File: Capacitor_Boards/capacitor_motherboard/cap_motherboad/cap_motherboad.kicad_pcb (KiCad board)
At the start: 2 copper layers, 180.5 x 92 mm, 14 parts, among them J1 Conn_01x02_Female, J10 Conn_01x02_Female, J11 Conn_01x02_Female, J12 Conn_01x02_Female, J2 Conn_01x02_Female, J3 Conn_01x02_Female, J4 Conn_01x02_Female, J5 Conn_01x02_Female, J6 Conn_01x02_Female, J7 Conn_01x02_Female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

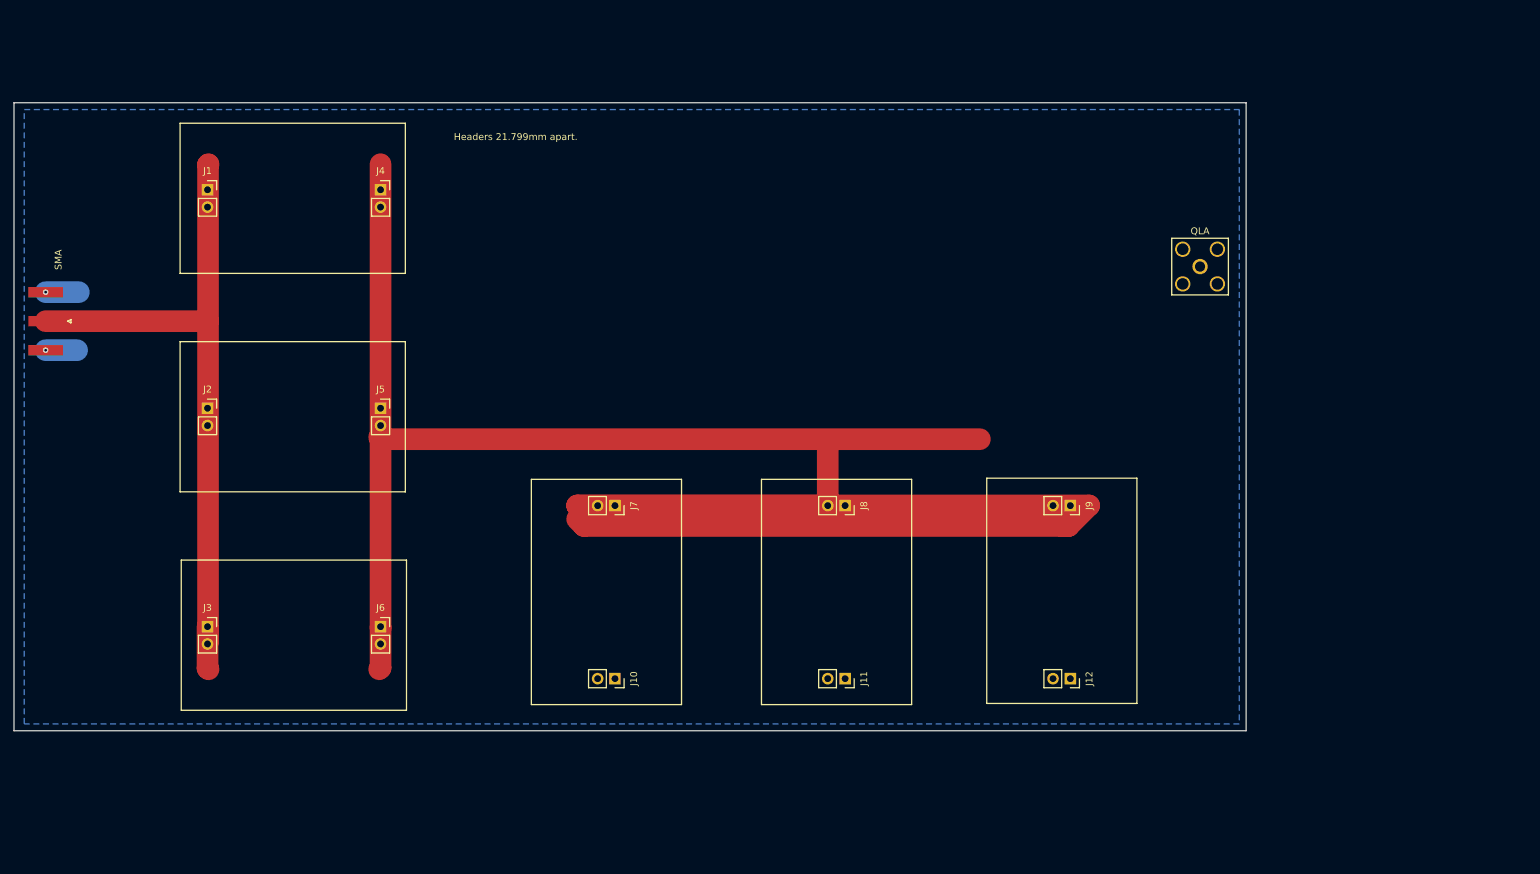
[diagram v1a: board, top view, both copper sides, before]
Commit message: Connected the QLA  connector
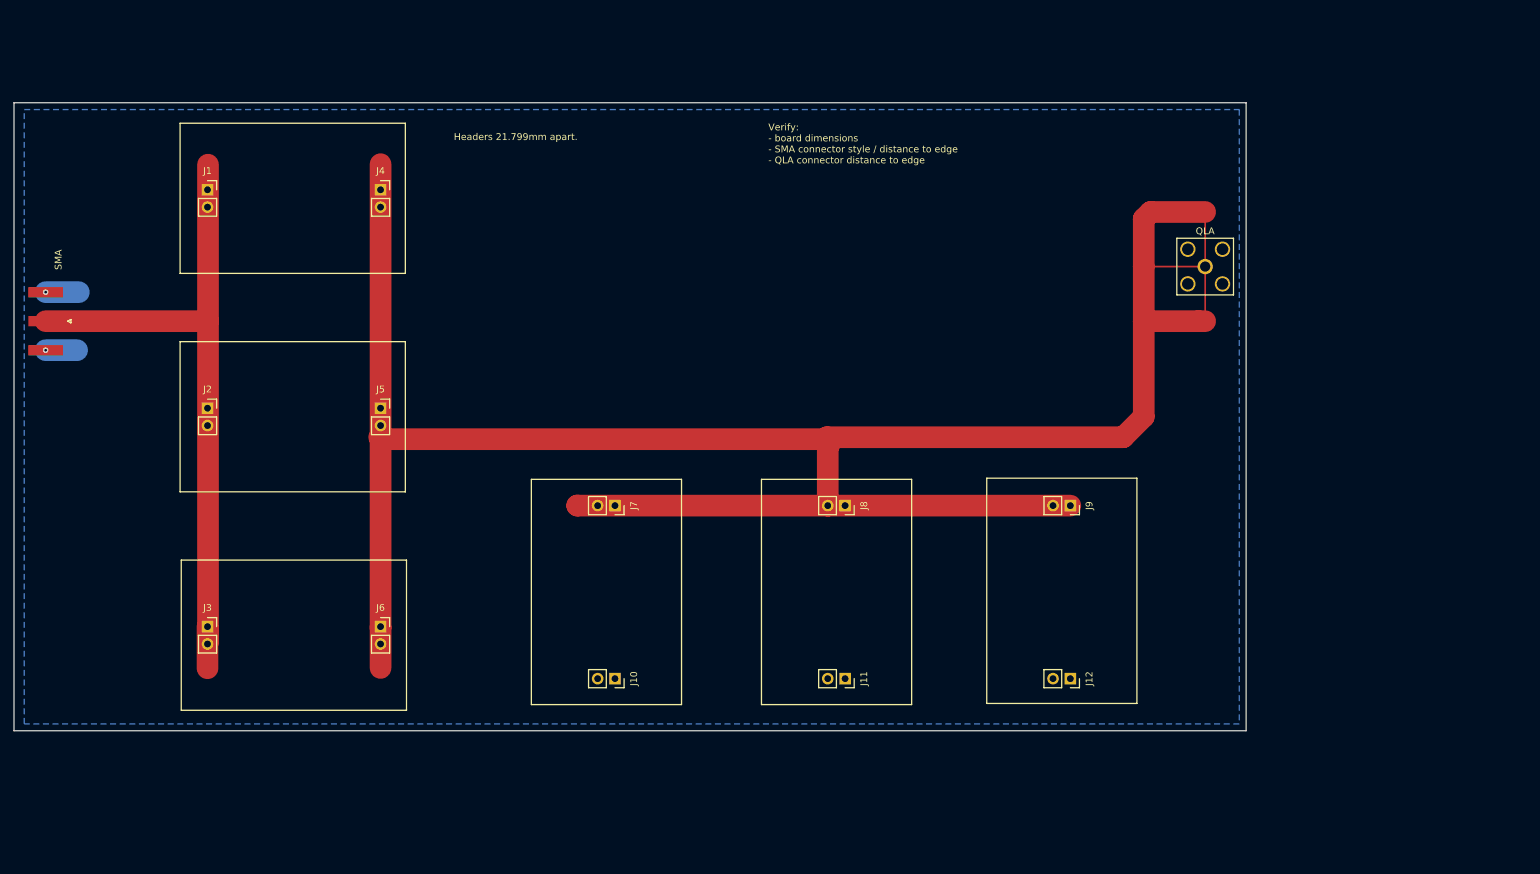
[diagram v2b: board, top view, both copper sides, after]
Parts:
- moved QLA 0.75 mm to (204.0, 62.0)
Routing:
- net Net-(J4-Pad1): track 359.6 -> 340.9 mm
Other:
- board text added: "Verify: - board dimensions - SMA connector style / distance to edge - QLA connector distance to edge"
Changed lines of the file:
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@@
   )
   (footprint "Connector_Coaxial:SMA_Amphenol_132203-12_Horizontal" (layer "F.Cu")
-    (at 203.25 62 -90)
+    (at 204 62 -90)
     (descr "https://www.amphenolrf.com/media/downloads/1769/132203-12.pdf")
     (tags "SMA THT Female Jack Horizontal")
@@
     (fp_line (start -3.175 -19.5) (end 3.175 -19.5) (layer "F.Fab") (width 0.1))
     (fp_line (start -3.175 -18) (end 3.175 -18.706) (layer "F.Fab") (width 0.1))
-    (pad "1" thru_hole circle (at 0 0 270) (size 2.25 2.25) (drill 1.5) (layers *.Cu *.Mask)
+    (pad "1" thru_hole circle (at 0 0 270) (size 2.25 2.25) (drill 1.5) (layers *.Cu *.Mask) (remove_unused_layers)
       (net 1 "Net-(J4-Pad1)") (pinfunction "In") (pintype "passive"))
-    (pad "2" thru_hole circle (at -2.54 -2.54 270) (size 2.25 2.25) (drill 1.7) (layers *.Cu *.Mask)
+    (pad "2" thru_hole circle (at -2.54 -2.54 270) (size 2.25 2.25) (drill 1.7) (layers *.Cu *.Mask) (remove_unused_layers)
       (net 2 "GND") (pinfunction "Ext") (pintype "passive"))
-    (pad "2" thru_hole circle (at 2.54 2.54) (size 2.25 2.25) (drill 1.7) (layers *.Cu *.Mask)
+    (pad "2" thru_hole circle (at 2.54 2.54) (size 2.25 2.25) (drill 1.7) (layers *.Cu *.Mask) (remove_unused_layers)
       (net 2 "GND") (pinfunction "Ext") (pintype "passive"))
-    (pad "2" thru_hole circle (at 2.54 -2.54 270) (size 2.25 2.25) (drill 1.7) (layers *.Cu *.Mask)
+    (pad "2" thru_hole circle (at 2.54 -2.54 270) (size 2.25 2.25) (drill 1.7) (layers *.Cu *.Mask) (remove_unused_layers)
       (net 2 "GND") (pinfunction "Ext") (pintype "passive"))
-    (pad "2" thru_hole circle (at -2.54 2.54 270) (size 2.25 2.25) (drill 1.7) (layers *.Cu *.Mask)
+    (pad "2" thru_hole circle (at -2.54 2.54 270) (size 2.25 2.25) (drill 1.7) (layers *.Cu *.Mask) (remove_unused_layers)
       (net 2 "GND") (pinfunction "Ext") (pintype "passive"))
     (model "${KICAD6_3DMODEL_DIR}/Connector_Coaxial.3dshapes/SMA_Amphenol_132203-12_Horizontal.wrl"
@@
   (gr_rect (start 53.83 73) (end 86.83 95) (layer "F.SilkS") (width 0.15) (fill none))
   (gr_rect (start 29.5 38) (end 210 130) (layer "Edge.Cuts") (width 0.1) (fill none))
+  (gr_text "Verify:\n- board dimensions\n- SMA connector style / distance to edge\n- QLA connector distance to edge" (at 140 44) (layer "F.SilkS")
+    (effects (font (size 1 1) (thickness 0.15)) (justify left))
+  )
   (gr_text "Headers 21.799mm apart." (at 103 43) (layer "F.SilkS")
     (effects (font (size 1 1) (thickness 0.15)))
   )
-  (segment (start 184 100) (end 183 100) (width 3.175) (layer "F.Cu") (net 1))
-  (segment (start 83.19914 120.80086) (end 83 121) (width 3.175) (layer "F.Cu") (net 1))
+  (segment (start 195 70) (end 195 62) (width 3.175) (layer "F.Cu") (net 1))
+  (segment (start 83 87) (end 83.29 87.29) (width 3.175) (layer "F.Cu") (net 1))
+  (segment (start 148.29 87.29) (end 149 88) (width 3.175) (layer "F.Cu") (net 1))
   (segment (start 148.71 97.0205) (end 112.0205 97.0205) (width 3.175) (layer "F.Cu") (net 1))
-  (segment (start 187 97) (end 184 100) (width 3.175) (layer "F.Cu") (net 1))
-  (segment (start 83 87) (end 83.29 87.29) (width 3.175) (layer "F.Cu") (net 1))
+  (segment (start 195 62) (end 195 55) (width 3.175) (layer "F.Cu") (net 1))
   (segment (start 83.19914 114.75) (end 83.19914 120.80086) (width 3.175) (layer "F.Cu") (net 1))
   (segment (start 83.19914 47) (end 83.19914 115) (width 3.175) (layer "F.Cu") (net 1))
+  (segment (start 203 70) (end 204 70) (width 3.175) (layer "F.Cu") (net 1))
   (segment (start 112.0205 97.0205) (end 112 97) (width 3.175) (layer "F.Cu") (net 1))
-  (segment (start 183 100) (end 113 100) (width 3.175) (layer "F.Cu") (net 1))
-  (segment (start 113 100) (end 112 99) (width 3.175) (layer "F.Cu") (net 1))
-  (segment (start 83.29 87.29) (end 171 87.29) (width 3.175) (layer "F.Cu") (net 1))
-  (segment (start 112 97) (end 187 97) (width 3.175) (layer "F.Cu") (net 1))
+  (segment (start 148.58 87) (end 192 87) (width 3.175) (layer "F.Cu") (net 1))
+  (segment (start 196 62) (end 204 62) (width 0.25) (layer "F.Cu") (net 1))
+  (segment (start 148.71 97.0205) (end 184.25 97.0205) (width 3.175) (layer "F.Cu") (net 1))
+  (segment (start 195 70) (end 203 70) (width 3.175) (layer "F.Cu") (net 1))
+  (segment (start 83.29 87.29) (end 148.29 87.29) (width 3.175) (layer "F.Cu") (net 1))
+  (segment (start 195 55) (end 196 54) (width 3.175) (layer "F.Cu") (net 1))
+  (segment (start 148.29 87.29) (end 148.58 87) (width 3.175) (layer "F.Cu") (net 1))
+  (segment (start 204 70) (end 204 54) (width 0.25) (layer "F.Cu") (net 1))
+  (segment (start 195 84) (end 195 70) (width 3.175) (layer "F.Cu") (net 1))
+  (segment (start 196 54) (end 204 54) (width 3.175) (layer "F.Cu") (net 1))
+  (segment (start 192 87) (end 195 84) (width 3.175) (layer "F.Cu") (net 1))
   (segment (start 148.71 97.0205) (end 148.71 88.29) (width 3.175) (layer "F.Cu") (net 1))
   (via (at 34.1375 74.25) (size 0.8) (drill 0.4) (layers "F.Cu" "B.Cu") (net 2))
@@
   (segment (start 34.1375 65.75) (end 39 65.75) (width 3.175) (layer "B.Cu") (net 2))
   (segment (start 34.1375 74.25) (end 38.75 74.25) (width 3.175) (layer "B.Cu") (net 2))
-  (segment (start 57.8505 120.8505) (end 58 121) (width 3.175) (layer "F.Cu") (net 3))
   (segment (start 57.925 70) (end 57.925 117) (width 3.175) (layer "F.Cu") (net 3))
   (segment (start 57.925 47.075) (end 57.925 70) (width 3.175) (layer "F.Cu") (net 3))
   (segment (start 57.8505 114.75) (end 57.8505 120.8505) (width 3.175) (layer "F.Cu") (net 3))
   (segment (start 34.1375 70) (end 57.925 70) (width 3.175) (layer "F.Cu") (net 3))
-  (segment (start 58 47) (end 57.925 47.075) (width 3.175) (layer "F.Cu") (net 3))
   (zone (net 2) (net_name "GND") (layer "B.Cu") (hatch edge 0.508)
     (connect_pads (clearance 0.508))

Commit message: Revised layout
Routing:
- net Net-(J4-Pad1): track 340.9 -> 344.6 mm
- net Net-(J1-Pad1): track 99.8 -> 97.6 mm
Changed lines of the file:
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@@
   (segment (start 83 87) (end 83.29 87.29) (width 3.175) (layer "F.Cu") (net 1))
   (segment (start 148.29 87.29) (end 149 88) (width 3.175) (layer "F.Cu") (net 1))
+  (segment (start 148.71 97.0205) (end 187.9795 97.0205) (width 3.175) (layer "F.Cu") (net 1))
   (segment (start 148.71 97.0205) (end 112.0205 97.0205) (width 3.175) (layer "F.Cu") (net 1))
   (segment (start 195 62) (end 195 55) (width 3.175) (layer "F.Cu") (net 1))
-  (segment (start 83.19914 114.75) (end 83.19914 120.80086) (width 3.175) (layer "F.Cu") (net 1))
-  (segment (start 83.19914 47) (end 83.19914 115) (width 3.175) (layer "F.Cu") (net 1))
   (segment (start 203 70) (end 204 70) (width 3.175) (layer "F.Cu") (net 1))
-  (segment (start 112.0205 97.0205) (end 112 97) (width 3.175) (layer "F.Cu") (net 1))
+  (segment (start 83.19914 47) (end 83.19914 121) (width 3.175) (layer "F.Cu") (net 1))
   (segment (start 148.58 87) (end 192 87) (width 3.175) (layer "F.Cu") (net 1))
   (segment (start 196 62) (end 204 62) (width 0.25) (layer "F.Cu") (net 1))
-  (segment (start 148.71 97.0205) (end 184.25 97.0205) (width 3.175) (layer "F.Cu") (net 1))
+  (segment (start 187.9795 97.0205) (end 188 97) (width 3.175) (layer "F.Cu") (net 1))
   (segment (start 195 70) (end 203 70) (width 3.175) (layer "F.Cu") (net 1))
   (segment (start 83.29 87.29) (end 148.29 87.29) (width 3.175) (layer "F.Cu") (net 1))
@@
   (segment (start 34.1375 65.75) (end 39 65.75) (width 3.175) (layer "B.Cu") (net 2))
   (segment (start 34.1375 74.25) (end 38.75 74.25) (width 3.175) (layer "B.Cu") (net 2))
-  (segment (start 57.925 70) (end 57.925 117) (width 3.175) (layer "F.Cu") (net 3))
   (segment (start 57.925 47.075) (end 57.925 70) (width 3.175) (layer "F.Cu") (net 3))
-  (segment (start 57.8505 114.75) (end 57.8505 120.8505) (width 3.175) (layer "F.Cu") (net 3))
   (segment (start 34.1375 70) (end 57.925 70) (width 3.175) (layer "F.Cu") (net 3))
+  (segment (start 57.925 70) (end 57.925 120.925) (width 3.175) (layer "F.Cu") (net 3))
   (zone (net 2) (net_name "GND") (layer "B.Cu") (hatch edge 0.508)
     (connect_pads (clearance 0.508))

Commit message: Finalized boards
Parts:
- added H1: MountingHole, MountingHole:MountingHole_3.2mm_M3, F.Cu at (71.9, 50.9)
- added H2: MountingHole, MountingHole:MountingHole_3.2mm_M3, F.Cu at (71.9, 108.0)
- added H3: MountingHole, MountingHole:MountingHole_3.2mm_M3, F.Cu at (173.5, 50.9)
- added H4: MountingHole, MountingHole:MountingHole_3.2mm_M3, F.Cu at (173.5, 108.0)
- added Strain Relief: MountingHole, MountingHole:MountingHole_3.2mm_M3, F.Cu at (172.7, 74.9)
- J1, J10, J11, J12, J2, J3, J4, J5, J6, J7, J8, J9: value Conn_01x02_Female -> Conn_01x05; footprint Connector_PinSocket_2.54mm:PinSocket_1x02_P2.54mm_Vertical -> Connector_PinSocket_2.54mm:PinSocket_1x05_P2.54mm_Vertical
- moved SMA1 138.5 mm to (172.4, 62.2), turned to 0 degrees
- moved QLA1 132.2 mm to (72.0, 69.0), turned to 90 degrees
- moved J3 32.7 mm to (85.9, 98.0)
- moved J2 29.1 mm to (85.9, 75.0)
- moved J1 28.1 mm to (85.9, 52.0)
- moved J12 26.0 mm to (170.4, 100.4)
- moved J6 24.6 mm to (101.2, 98.0)
- moved J10 22.7 mm to (123.0, 100.4)
- moved J11 22.5 mm to (146.7, 100.4)
- moved J5 19.6 mm to (101.2, 75.0)
- moved J9 18.3 mm to (170.4, 85.1)
- moved J4 18.0 mm to (101.2, 52.0)
- moved J7 13.1 mm to (123.0, 85.1)
- moved J8 12.8 mm to (146.7, 85.1)
- renumbered QLA to QLA1, SMA to SMA1
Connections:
- QLA1 pad 1: Net-(J4-Pad1) -> Net-(J1-Pad1)
- SMA1 pad 1: Net-(J1-Pad1) -> Net-(J4-Pad1)
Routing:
- net Net-(J4-Pad1): track 344.6 -> 183.4 mm
- net Net-(J1-Pad1): track 97.6 -> 118.4 mm
- net GND: track 9.47 -> 0.00 mm, vias 2 -> 6
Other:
- board size 180.5 x 92 mm -> 112.4 x 67.9 mm
- board text removed: "Headers 21.799mm apart."
- board text removed: "Verify: - board dimensions - SMA connector style / distance to edge - QLA connector distance to edge"
